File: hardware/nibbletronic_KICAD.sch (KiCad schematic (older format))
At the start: 18 parts, among them P1 DIN_5, SW1 SWITCH_INV, SW2 SWITCH_INV, SW3 SWITCH_INV, SW4 SWITCH_INV, SW5 SWITCH_INV, SW6 SW_PUSH, SW7 Switch_SPDT_x2, U1 Arduino_micro, U2 MPX5010DP, U3 Joystick

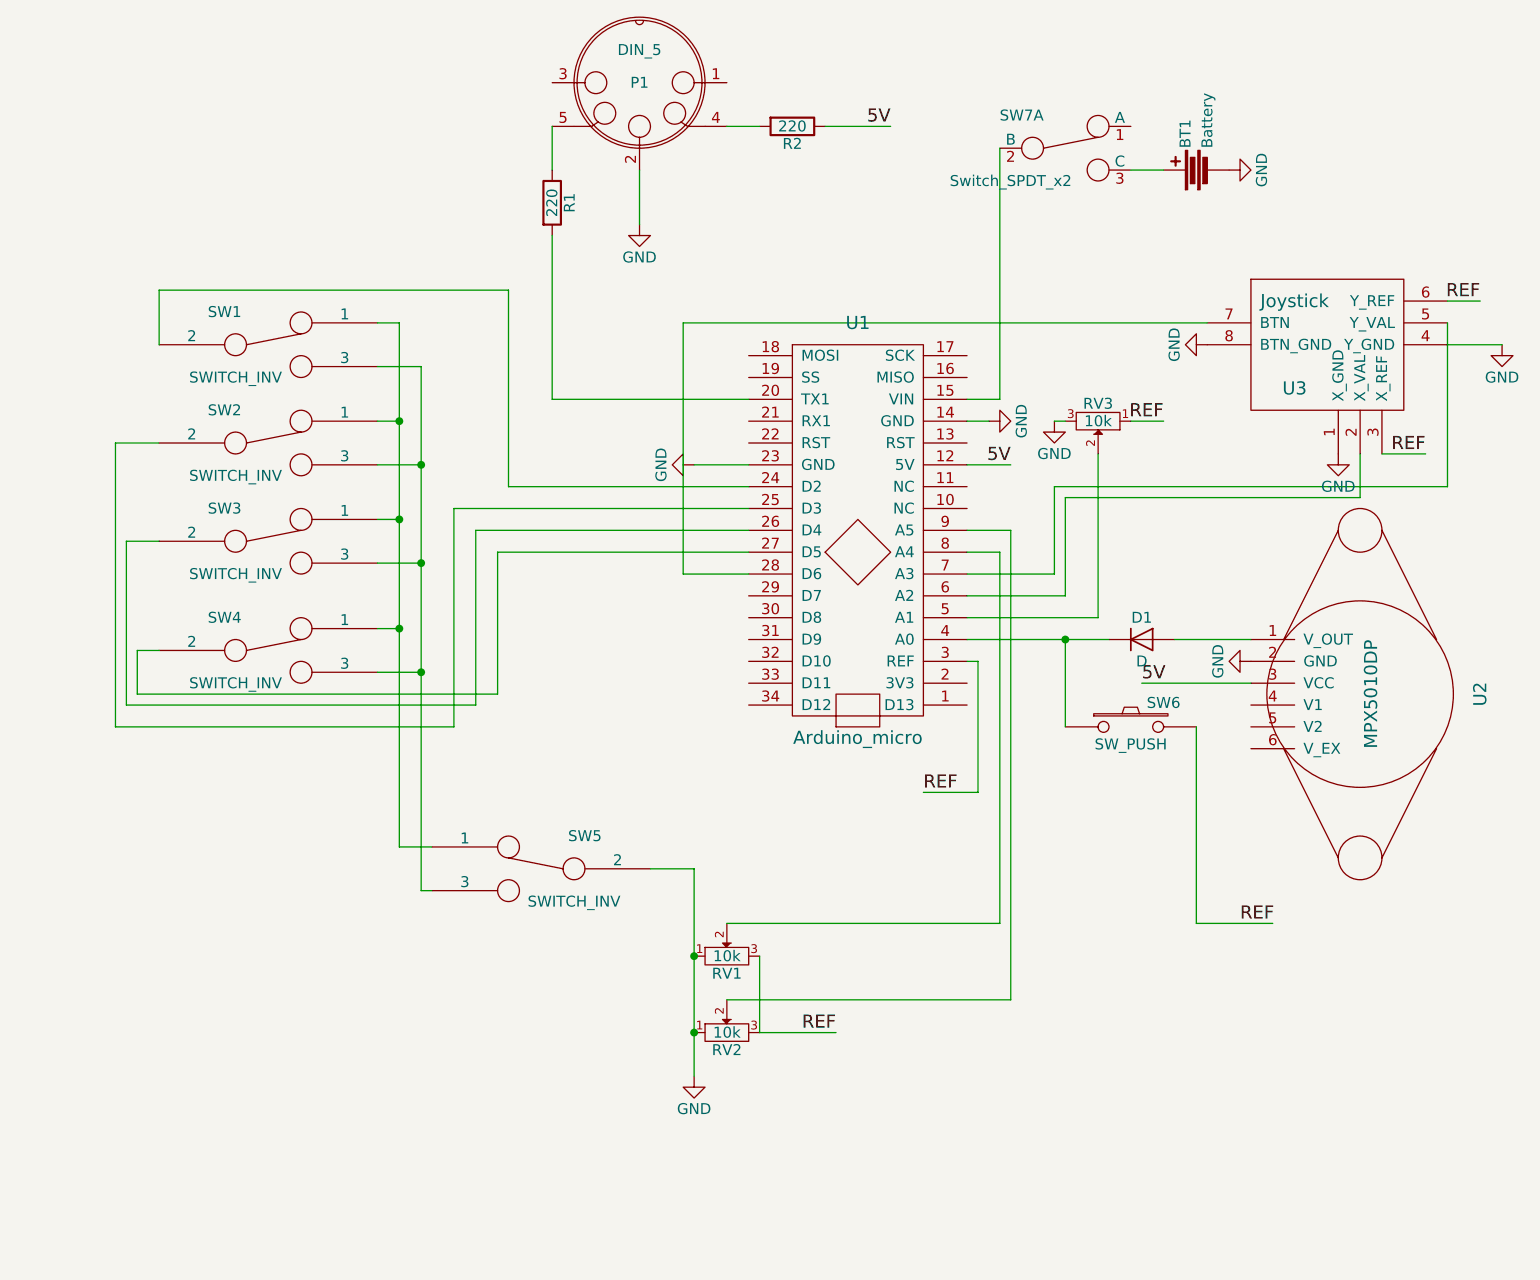
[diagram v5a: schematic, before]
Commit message: Hardware 2.0: Touch Buttons and a RotEnc
- Microswitches are replaced by touch sensors with a dedicated IC
- Octave slider has been replaced by two touch sensors
- Added a Rotenc at pins D10-12 and D9 for the Button.
- I2C and all remaining pins (A1, D4, D5, D8, D13), as well as GND, Ref,
3.3/5V have been broken out for easier access
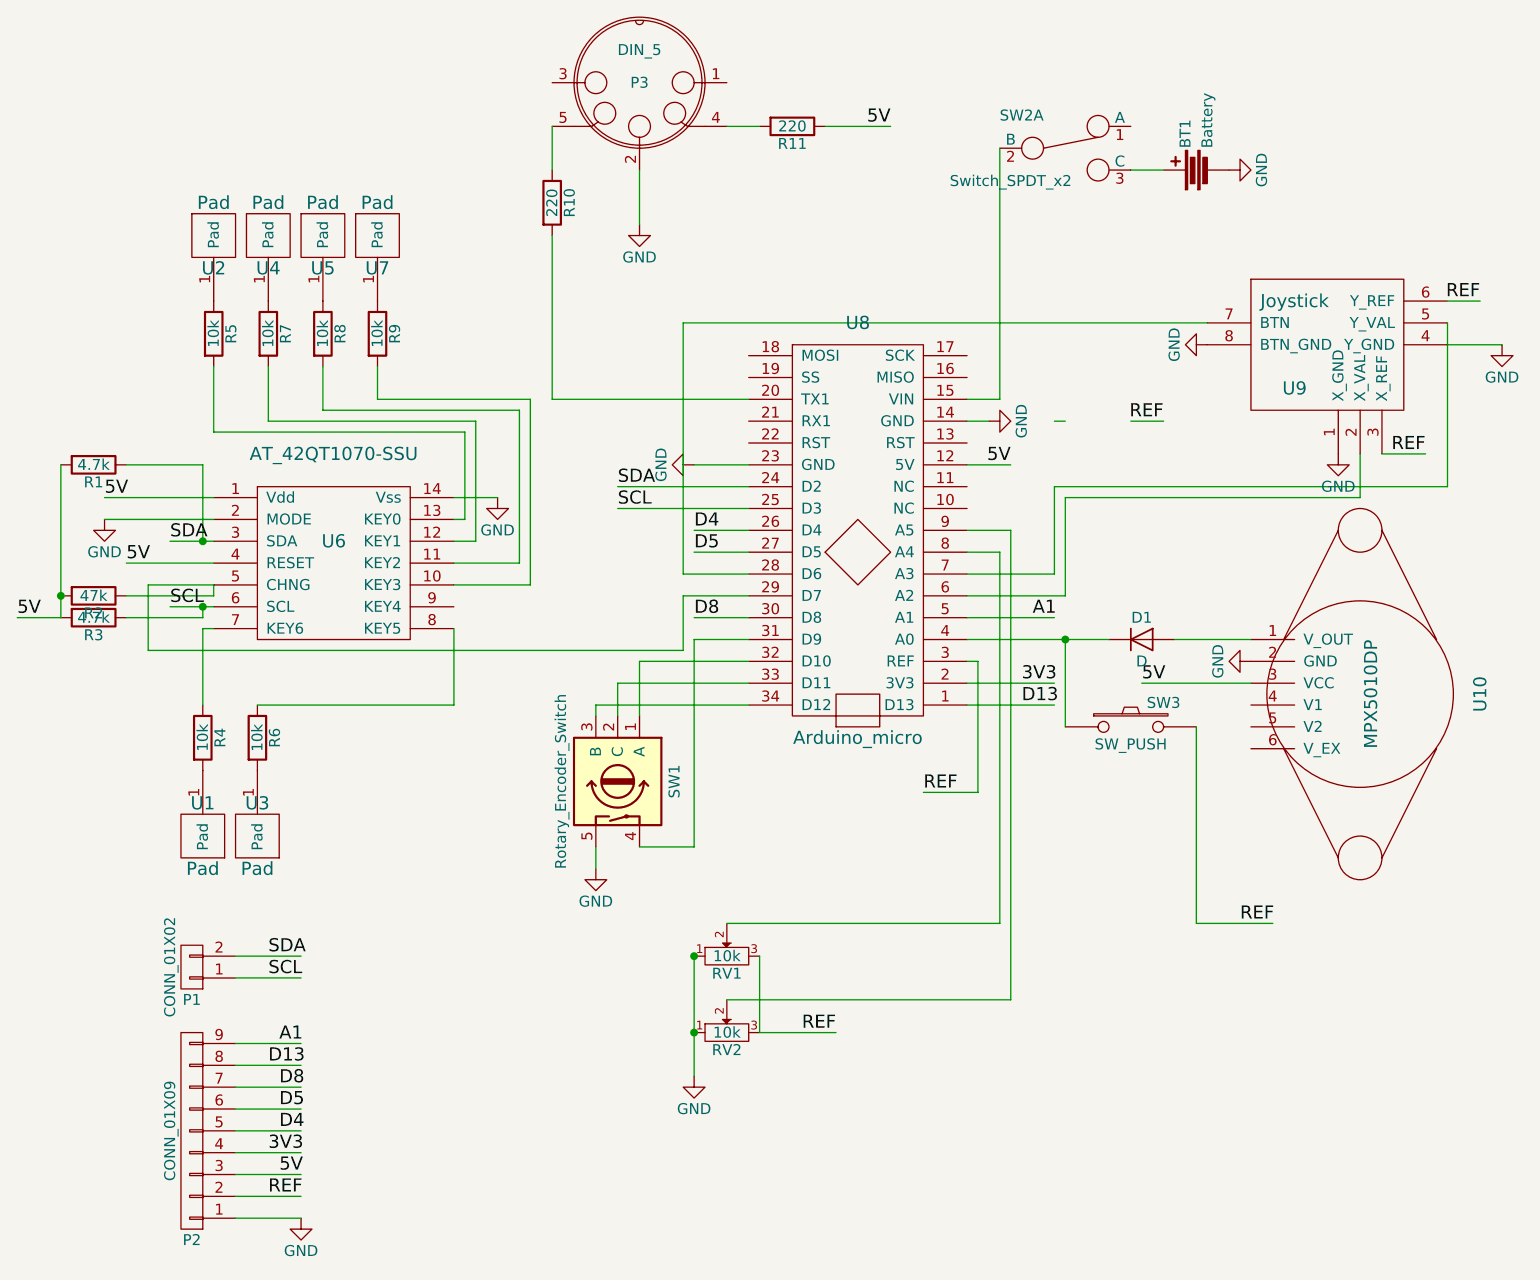
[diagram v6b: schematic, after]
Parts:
- removed RV3: 10k, CustomParts:ALPS_402125, symbol POT-RESCUE-nibbletronic_KICAD
- removed SW1, SW2, SW3, SW4: SWITCH_INV, CustomParts:MARQUARDT_SPDT, symbol SWITCH_INV
- removed SW5: SWITCH_INV, CustomParts:ESP40XX, symbol SWITCH_INV
- added P1: CONN_01X02, Pin_Headers:Pin_Header_Straight_2x01_Pitch2.54mm, symbol CONN_01X02
- added P2: CONN_01X09, Pin_Headers:Pin_Header_Straight_1x09_Pitch2.54mm, symbol CONN_01X09
- added R1, R3: 4.7k, Resistors_SMD:R_0805_HandSoldering, symbol R
- added R2: 47k, Resistors_SMD:R_0805_HandSoldering, symbol R
- added R4, R5, R6, R7, R8, R9: 10k, Resistors_SMD:R_0805_HandSoldering, symbol R
- added SW1: Rotary_Encoder_Switch, CustomParts:ALPS-STEC12E, symbol Rotary_Encoder_Switch
- added U1, U2, U3, U4, U5, U7: Pad, CustomParts:Pad, symbol Pad
- added U6: AT_42QT1070-SSU, Housings_SOIC:SOIC-14_3.9x8.7mm_Pitch1.27mm, symbol AT_42QT1070-SSU
- SW3: renamed from SW6; footprint CustomParts:SMD_Pushbutton -> Buttons_Switches_SMD:SW_SPST_PTS645
- renumbered P1 to P3, R1 to R10, R2 to R11, SW7 to SW2, U2 to U10, U1 to U8, U3 to U9
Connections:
- net labels added: 3V3, A1, D13, D4, D5, D8, SCL, SDA
- wire segments 80 -> 114
